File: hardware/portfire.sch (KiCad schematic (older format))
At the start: 52 parts, among them IC4 25AA02E48, IC5 STM32F4xxVxTx, P1 1, P10 10, P11 11, P12 12, P13 13, P14 14, P15 15, P16 16, P17 17, P18 18, P19 19, P2 2, P20 20, P21 21, P22 22, P23 23, P24 24, P25 25, P26 26, P27 27, P28 28, P29 29, P3 3, P30 30, P4 4, P5 5, P6 6, P7 7, P8 8, P9 9

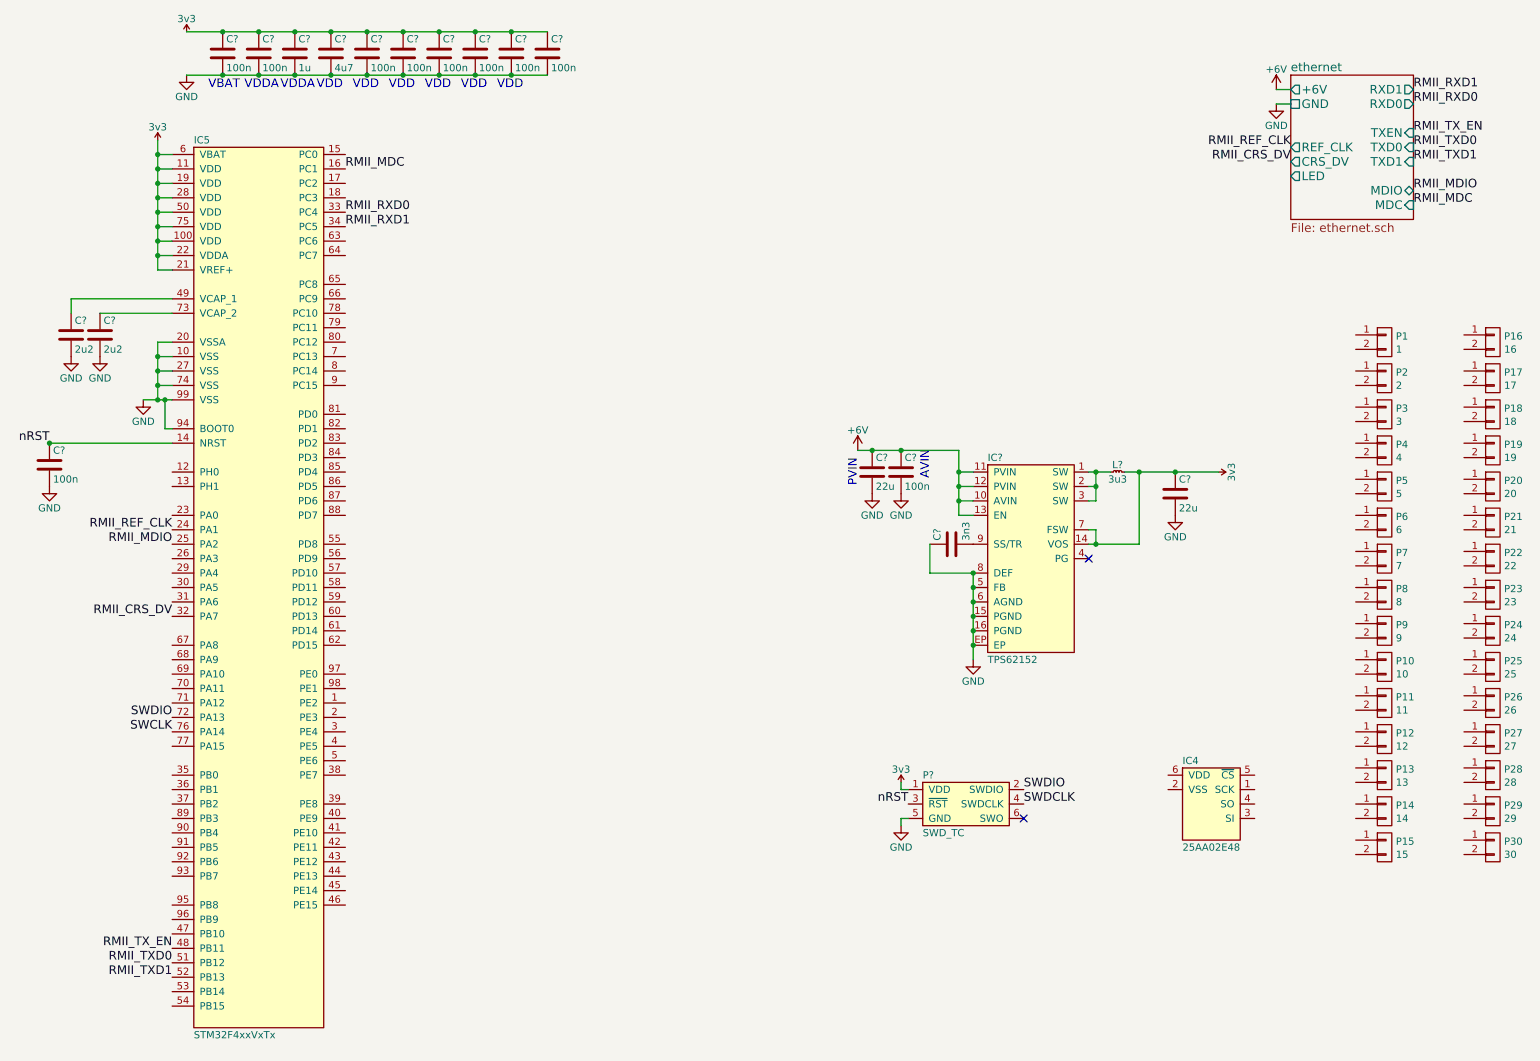
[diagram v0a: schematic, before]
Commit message: Added firing switch transistors
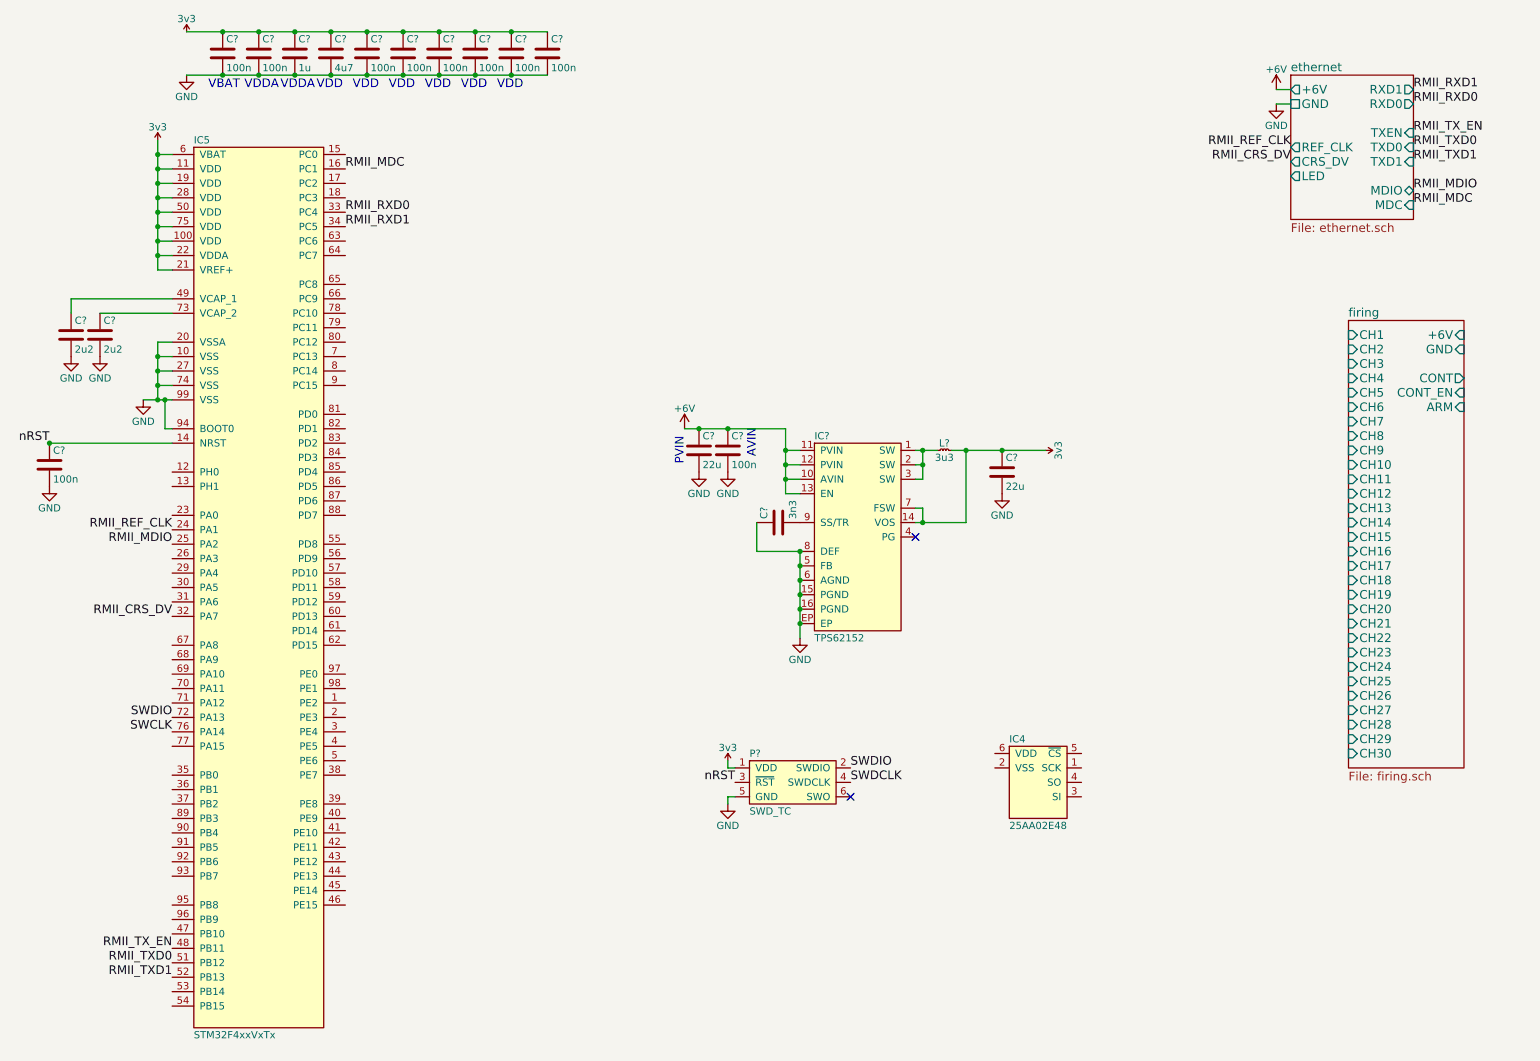
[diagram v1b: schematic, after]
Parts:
- removed P1: 1, hardware:PTSA0,52-2,5-z, symbol CONN_01X02
- removed P10: 10, hardware:PTSA0,52-2,5-z, symbol CONN_01X02
- removed P11: 11, hardware:PTSA0,52-2,5-z, symbol CONN_01X02
- removed P12: 12, hardware:PTSA0,52-2,5-z, symbol CONN_01X02
- removed P13: 13, hardware:PTSA0,52-2,5-z, symbol CONN_01X02
- removed P14: 14, hardware:PTSA0,52-2,5-z, symbol CONN_01X02
- removed P15: 15, hardware:PTSA0,52-2,5-z, symbol CONN_01X02
- removed P16: 16, hardware:PTSA0,52-2,5-z, symbol CONN_01X02
- removed P17: 17, hardware:PTSA0,52-2,5-z, symbol CONN_01X02
- removed P18: 18, hardware:PTSA0,52-2,5-z, symbol CONN_01X02
- removed P19: 19, hardware:PTSA0,52-2,5-z, symbol CONN_01X02
- removed P2: 2, hardware:PTSA0,52-2,5-z, symbol CONN_01X02
- removed P20: 20, hardware:PTSA0,52-2,5-z, symbol CONN_01X02
- removed P21: 21, hardware:PTSA0,52-2,5-z, symbol CONN_01X02
- removed P22: 22, hardware:PTSA0,52-2,5-z, symbol CONN_01X02
- removed P23: 23, hardware:PTSA0,52-2,5-z, symbol CONN_01X02
- removed P24: 24, hardware:PTSA0,52-2,5-z, symbol CONN_01X02
- removed P25: 25, hardware:PTSA0,52-2,5-z, symbol CONN_01X02
- removed P26: 26, hardware:PTSA0,52-2,5-z, symbol CONN_01X02
- removed P27: 27, hardware:PTSA0,52-2,5-z, symbol CONN_01X02
- removed P28: 28, hardware:PTSA0,52-2,5-z, symbol CONN_01X02
- removed P29: 29, hardware:PTSA0,52-2,5-z, symbol CONN_01X02
- removed P3: 3, hardware:PTSA0,52-2,5-z, symbol CONN_01X02
- removed P30: 30, hardware:PTSA0,52-2,5-z, symbol CONN_01X02
- removed P4: 4, hardware:PTSA0,52-2,5-z, symbol CONN_01X02
- removed P5: 5, hardware:PTSA0,52-2,5-z, symbol CONN_01X02
- removed P6: 6, hardware:PTSA0,52-2,5-z, symbol CONN_01X02
- removed P7: 7, hardware:PTSA0,52-2,5-z, symbol CONN_01X02
- removed P8: 8, hardware:PTSA0,52-2,5-z, symbol CONN_01X02
- removed P9: 9, hardware:PTSA0,52-2,5-z, symbol CONN_01X02
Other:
- moved on the sheet: C?, IC4, IC?, L?, P?

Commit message: Firing matrix and CC SMPS
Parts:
- removed C?: 22u, agg:1206, symbol C
- added C117: 22u, agg:1206, symbol C
- C114: renamed from C?; Farnell 2118135 -> 1797010
- gave numbers to parts that had none: 18
- renumbered IC5 to IC101, IC4 to IC103
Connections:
- net 3v3: now also C117.1
- net GND: now also C117.2

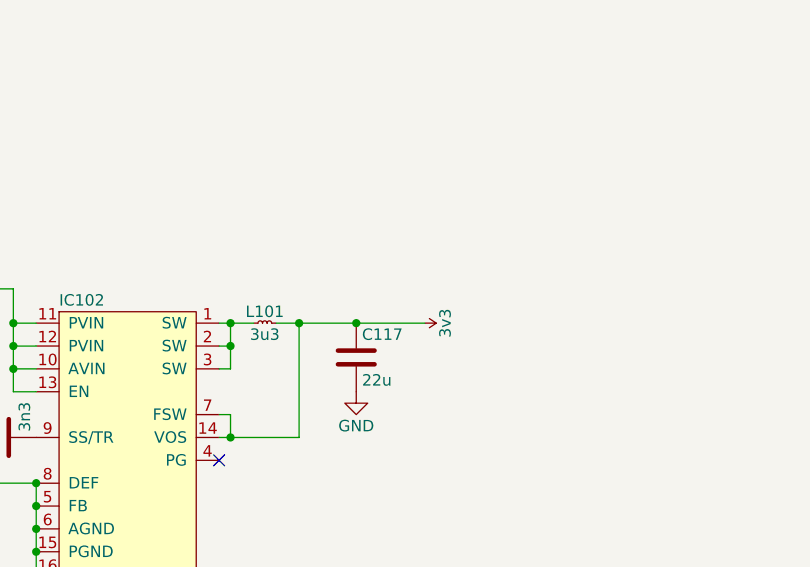
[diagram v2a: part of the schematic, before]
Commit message: aux power, test points
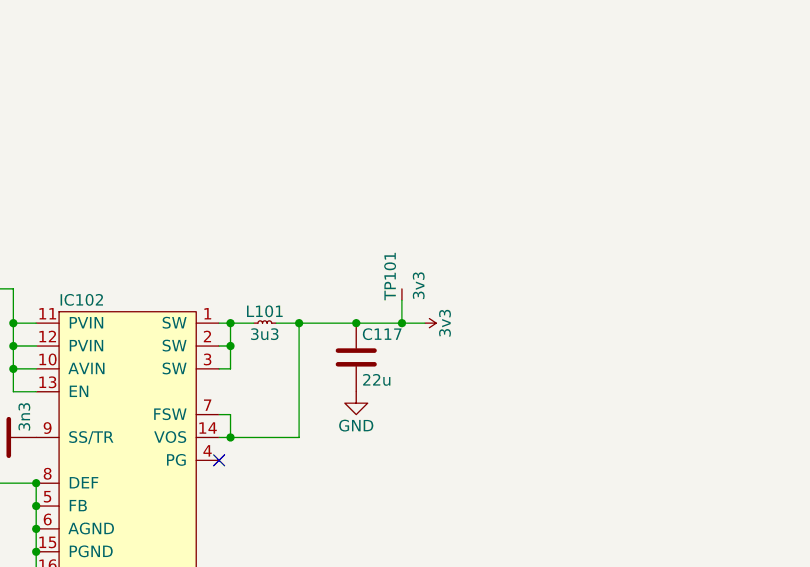
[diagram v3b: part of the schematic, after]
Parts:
- added TP101: 3v3, hardware:Test_point_mini, symbol TESTPAD
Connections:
- net 3v3: now also TP101.1 (TP)
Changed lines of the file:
@@
 RMII_RXD0
 $Comp
-L +6V #PWR116
+L +6V #PWR01
 U 1 1 57F2FE2A
 P 9250 1050
-F 0 "#PWR116" H 9250 900 50  0001 C CNN
+F 0 "#PWR01" H 9250 900 50  0001 C CNN
 F 1 "+6V" H 9250 1190 50  0000 C CNN
 F 2 "" H 9250 1050 50  0000 C CNN
@@
 	9250 1050 9350 1050
 $Comp
-L GND #PWR117
+L GND #PWR02
 U 1 1 57F2FF50
 P 9250 1150
-F 0 "#PWR117" H 9250 900 50  0001 C CNN
+F 0 "#PWR02" H 9250 900 50  0001 C CNN
 F 1 "GND" H 9250 1000 50  0000 C CNN
 F 2 "" H 9250 1150 50  0000 C CNN
@@
 $EndComp
 $Comp
-L +6V #PWR108
+L +6V #PWR03
 U 1 1 57F05FAB
 P 5150 3400
-F 0 "#PWR108" H 5150 3250 50  0001 C CNN
+F 0 "#PWR03" H 5150 3250 50  0001 C CNN
 F 1 "+6V" H 5150 3540 50  0000 C CNN
 F 2 "" H 5150 3400 50  0000 C CNN
@@
 $EndComp
 $Comp
-L GND #PWR109
+L GND #PWR04
 U 1 1 57F09927
 P 5250 3700
-F 0 "#PWR109" H 5250 3450 50  0001 C CNN
+F 0 "#PWR04" H 5250 3450 50  0001 C CNN
 F 1 "GND" H 5250 3550 50  0000 C CNN
 F 2 "" H 5250 3700 50  0000 C CNN
@@
 $EndComp
 $Comp
-L GND #PWR110
+L GND #PWR05
 U 1 1 57F09A10
 P 5450 3700
-F 0 "#PWR110" H 5450 3450 50  0001 C CNN
+F 0 "#PWR05" H 5450 3450 50  0001 C CNN
 F 1 "GND" H 5450 3550 50  0000 C CNN
 F 2 "" H 5450 3700 50  0000 C CNN
@@
 Connection ~ 5950 4750
 $Comp
-L GND #PWR113
+L GND #PWR06
 U 1 1 57F0A67A
 P 5950 4850
-F 0 "#PWR113" H 5950 4600 50  0001 C CNN
+F 0 "#PWR06" H 5950 4600 50  0001 C CNN
 F 1 "GND" H 5950 4700 50  0000 C CNN
 F 2 "" H 5950 4850 50  0000 C CNN
@@
 Connection ~ 7350 3550
 $Comp
-L 3v3 #PWR115
+L 3v3 #PWR07
 U 1 1 57F10D6C
 P 7650 3550
-F 0 "#PWR115" H 7650 3660 50  0001 L CNN
+F 0 "#PWR07" H 7650 3660 50  0001 L CNN
 F 1 "3v3" H 7650 3640 50  0000 C CNN
 F 2 "" H 7650 3550 60  0001 C CNN
@@
 $EndComp
 $Comp
-L GND #PWR114
+L GND #PWR08
 U 1 1 57F10E60
 P 7350 3850
-F 0 "#PWR114" H 7350 3600 50  0001 C CNN
+F 0 "#PWR08" H 7350 3600 50  0001 C CNN
 F 1 "GND" H 7350 3700 50  0000 C CNN
 F 2 "" H 7350 3850 50  0000 C CNN
@@
 $EndComp
 $Comp
-L 3v3 #PWR105
+L 3v3 #PWR09
 U 1 1 57F1B4C2
 P 1500 1400
-F 0 "#PWR105" H 1500 1510 50  0001 L CNN
+F 0 "#PWR09" H 1500 1510 50  0001 L CNN
 F 1 "3v3" H 1500 1490 50  0000 C CNN
 F 2 "" H 1500 1400 60  0001 C CNN
@@
 Connection ~ 1500 2200
 $Comp
-L 3v3 #PWR106
+L 3v3 #PWR010
 U 1 1 57F1C37E
 P 1700 650
-F 0 "#PWR106" H 1700 760 50  0001 L CNN
+F 0 "#PWR010" H 1700 760 50  0001 L CNN
 F 1 "3v3" H 1700 740 50  0000 C CNN
 F 2 "" H 1700 650 60  0001 C CNN
@@
 $EndComp
 $Comp
-L GND #PWR107
+L GND #PWR011
 U 1 1 57F1E348
 P 1700 950
-F 0 "#PWR107" H 1700 700 50  0001 C CNN
+F 0 "#PWR011" H 1700 700 50  0001 C CNN
 F 1 "GND" H 1700 800 50  0000 C CNN
 F 2 "" H 1700 950 50  0000 C CNN
@@
 	900  2500 1600 2500
 $Comp
-L GND #PWR103
+L GND #PWR012
 U 1 1 57F2BB16
 P 1100 2900
-F 0 "#PWR103" H 1100 2650 50  0001 C CNN
+F 0 "#PWR012" H 1100 2650 50  0001 C CNN
 F 1 "GND" H 1100 2750 50  0000 C CNN
 F 2 "" H 1100 2900 50  0000 C CNN
@@
 $EndComp
 $Comp
-L GND #PWR102
+L GND #PWR013
 U 1 1 57F2BC2C
 P 900 2900
-F 0 "#PWR102" H 900 2650 50  0001 C CNN
+F 0 "#PWR013" H 900 2650 50  0001 C CNN
 F 1 "GND" H 900 2750 50  0000 C CNN
 F 2 "" H 900 2900 50  0000 C CNN
@@
 	1700 950  4200 950
 $Comp
-L GND #PWR104
+L GND #PWR014
 U 1 1 57F2D2C0
 P 1400 3200
-F 0 "#PWR104" H 1400 2950 50  0001 C CNN
+F 0 "#PWR014" H 1400 2950 50  0001 C CNN
 F 1 "GND" H 1400 3050 50  0000 C CNN
 F 2 "" H 1400 3200 50  0000 C CNN
@@
 	750  3500 1600 3500
 $Comp
-L GND #PWR101
+L GND #PWR015
 U 1 1 57F30601
 P 750 3800
-F 0 "#PWR101" H 750 3550 50  0001 C CNN
+F 0 "#PWR015" H 750 3550 50  0001 C CNN
 F 1 "GND" H 750 3650 50  0000 C CNN
 F 2 "" H 750 3800 50  0000 C CNN
@@
 $EndComp
 $Comp
-L 3v3 #PWR111
+L 3v3 #PWR016
 U 1 1 57F32567
 P 5450 5700
-F 0 "#PWR111" H 5450 5810 50  0001 L CNN
+F 0 "#PWR016" H 5450 5810 50  0001 L CNN
 F 1 "3v3" H 5450 5790 50  0000 C CNN
 F 2 "" H 5450 5700 60  0001 C CNN
@@
 nRST
 $Comp
-L GND #PWR112
+L GND #PWR017
 U 1 1 57F329FA
 P 5450 6000
-F 0 "#PWR112" H 5450 5750 50  0001 C CNN
+F 0 "#PWR017" H 5450 5750 50  0001 C CNN
 F 1 "GND" H 5450 5850 50  0000 C CNN
 F 2 "" H 5450 6000 50  0000 C CNN
@@
 	1    0    0    -1
 $EndComp
+$Comp
+L TESTPAD TP101
+U 1 1 57F39F58
+P 7550 3450
+F 0 "TP101" H 7550 3500 50  0000 L CNN
+F 1 "3v3" H 7550 3375 50  0000 L CNN
+F 2 "hardware:Test_point_mini" H 7550 3300 50  0001 L CNN
+F 3 "" H 7550 3450 50  0001 C CNN
+	1    7550 3450
+	0    -1   -1   0
+$EndComp
+Wire Wire Line
+	7550 3450 7550 3550
+Connection ~ 7550 3550
 $EndSCHEMATC

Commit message: Added aux bus
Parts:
- added C118, C120: 2u2, agg:0603, symbol C
- added C119: 100n, agg:0603, symbol C
- added IC104: ADP3335, agg:MSOP-8, symbol ADP3335
- added IC105: SNx5176B, agg:SOIC-8, symbol SNx5176B
- added P102, P103: AUX_BUS_RX, agg:B02B-PASK, symbol CONN_01X02
- C106: Farnell (none) -> 9227776
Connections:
- net +6V: now also C118.1, IC104.6 (SD), IC104.7 (IN), IC104.8 (IN)
- net GND: now also C118.2, C119.2, C120.2, IC104.4 (GND), IC105.2 (~RE), IC105.3 (DE), IC105.5 (GND)
- new net: IC105.6 (A), P102.1 (P1), P103.1 (P1)
- new net: IC105.7 (B), P102.2 (P2), P103.2 (P2)
- new net +5V: C119.1, C120.1, IC104.1 (OUT), IC104.2 (OUT), IC104.3 (OUT), IC105.8 (VCC)
- new net AUX_BUS_RX: IC105.1 (R)
- no-connect marks 2 -> 4

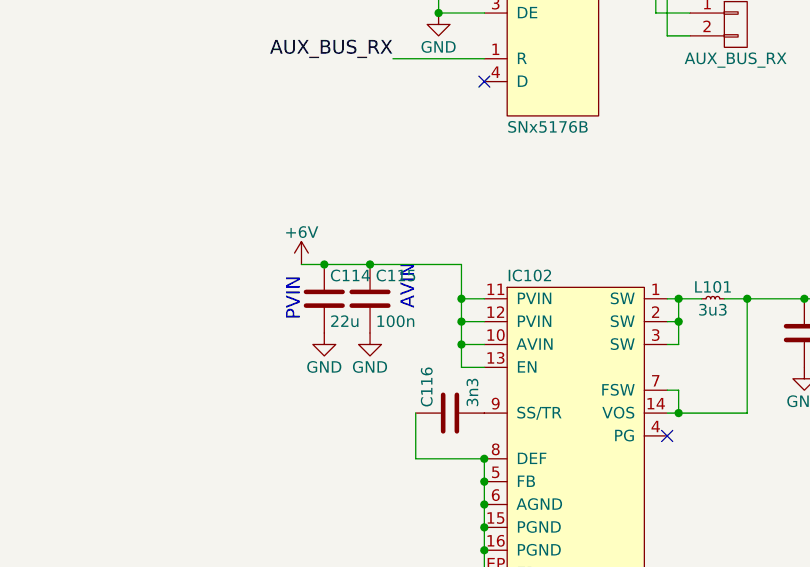
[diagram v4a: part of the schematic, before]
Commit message: Fixed schematic part with derpy path
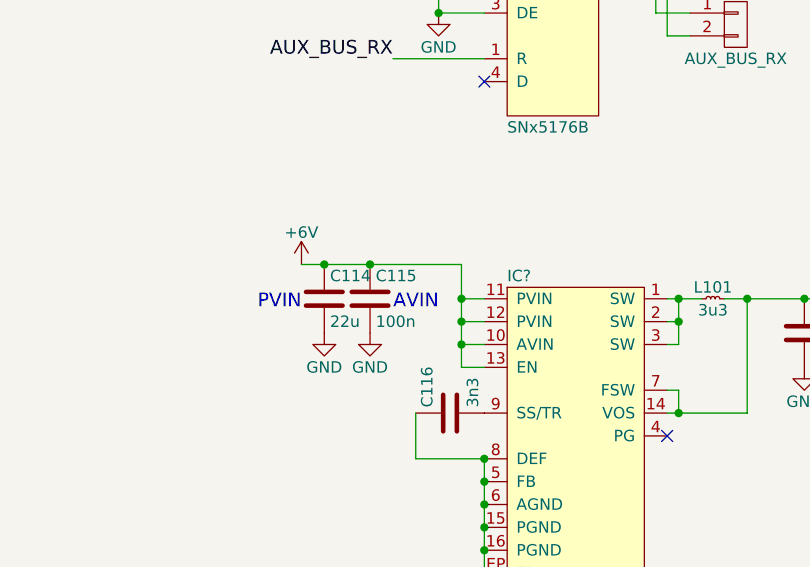
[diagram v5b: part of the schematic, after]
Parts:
- removed IC102: TPS62152, agg:QFN-16-EP-TI, symbol TPS62152
- added IC?: TPS62152, agg:QFN-16-EP-TI, symbol TPS62152
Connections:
- net +6V: now also IC?.10 (AVIN), IC?.11 (PVIN), IC?.12 (PVIN), IC?.13 (EN)
- net 3v3: now also IC?.14 (VOS), IC?.7 (FSW)
- net GND: now also IC?.15 (PGND), IC?.16 (PGND), IC?.5 (FB), IC?.6 (AGND), IC?.8 (DEF), IC?.EP
- net at L101.1: now also IC?.1 (SW), IC?.2 (SW), IC?.3 (SW)
- net at C116.2: now also IC?.9 (SS/TR)
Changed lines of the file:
@@
 LIBS:valves
 LIBS:agg-kicad
-LIBS:tps92512
 LIBS:portfire-cache
 EELAYER 25 0
@@
 	9250 1150 9350 1150
 $Comp
-L TPS62152 IC102
-U 1 1 57F0558B
-P 6350 4150
-F 0 "IC102" H 6050 4850 50  0000 L CNN
-F 1 "TPS62152" H 6050 3450 50  0000 L CNN
-F 2 "agg:QFN-16-EP-TI" H 6050 3350 50  0001 L CNN
-F 3 "http://www.ti.com/lit/ds/symlink/tps62152.pdf" H 6050 3250 50  0001 L CNN
-F 4 "2382918" H 6050 3150 50  0001 L CNN "Farnell"
-	1    6350 4150
-	1    0    0    -1
-$EndComp
-$Comp
 L +6V #PWR108
 U 1 1 57F05FAB
@@
 $EndComp
 NoConn ~ 6750 4150
-Text Notes 5150 3650 1    60   ~ 0
+Text Notes 5150 3600 2    60   ~ 0
 PVIN
-Text Notes 5650 3600 1    60   ~ 0
+Text Notes 5750 3600 2    60   ~ 0
 AVIN
 Wire Wire Line
@@
 Text Label 3150 3150 0    60   ~ 0
 AUX_BUS_RX
+$Comp
+L TPS62152 IC?
+U 1 1 57F422C0
+P 6350 4150
+F 0 "IC?" H 6050 4850 50  0000 L CNN
+F 1 "TPS62152" H 6050 3450 50  0000 L CNN
+F 2 "agg:QFN-16-EP-TI" H 6050 3350 50  0001 L CNN
+F 3 "http://www.ti.com/lit/ds/symlink/tps62152.pdf" H 6050 3250 50  0001 L CNN
+F 4 "2382918" H 6050 3150 50  0001 L CNN "Farnell"
+	1    6350 4150
+	1    0    0    -1
+$EndComp
 $EndSCHEMATC
